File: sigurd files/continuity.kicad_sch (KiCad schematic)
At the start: 26 parts, among them U3 VN7050ASTR, U4 VN7050ASTR, U5 VN7050ASTR

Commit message: funny fortnite
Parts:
- added R33: 47k, Resistor_SMD:R_0603_1608Metric_Pad0.98x0.95mm_HandSolder, symbol Device:R_Small
- R27, R28, R32: footprint Resistor_SMD:R_0603_1608Metric -> Resistor_SMD:R_0603_1608Metric_Pad0.98x0.95mm_HandSolder
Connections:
- net JMPR: now also R33.1; no longer D3.2 (A)
- new net: D3.2 (A), R33.2
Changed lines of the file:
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@@
-	(wire
-		(pts
-			(xy 106.68 128.27) (xy 106.68 133.35)
-		)
-		(stroke
-			(width 0)
-			(type default)
-		)
-	)
 	(wire
 		(pts
@@
 	)
 	(symbol
-		(lib_id "Device:R_Small")
-		(at 102.87 95.25 270)
-		(unit 1)
-		(exclude_from_sim no)
-		(in_bom yes)
-		(on_board yes)
-		(dnp no)
-		(fields_autoplaced yes)
-		(property "Reference" "R28"
-			(at 102.87 90.17 90)
-			(effects
-				(font
-					(size 1.27 1.27)
-				)
-			)
-		)
-		(property "Value" "47k"
-			(at 102.87 92.71 90)
-			(effects
-				(font
-					(size 1.27 1.27)
-				)
-			)
-		)
-		(property "Footprint" "Resistor_SMD:R_0603_1608Metric"
-			(at 102.87 95.25 0)
-			(effects
-				(font
-					(size 1.27 1.27)
-				)
-				(hide yes)
-			)
-		)
-		(property "Datasheet" "~"
-			(at 102.87 95.25 0)
-			(effects
-				(font
-					(size 1.27 1.27)
-				)
-				(hide yes)
-			)
-		)
-		(property "Description" ""
-			(at 102.87 95.25 0)
-			(effects
-				(font
-					(size 1.27 1.27)
-				)
-				(hide yes)
-			)
-		)
-		(pin "1"
-		)
-		(pin "2"
-		)
-		(instances
-			(project "SIGURD"
-				(path "/a4a592a3-08d1-41ec-9dda-18a75407e2f6/8efa7d73-8cac-417d-b1a4-5e5d923803a7"
-					(reference "R28")
-					(unit 1)
-				)
-			)
-		)
-	)
-	(symbol
 		(lib_name "Earth_12")
 		(lib_id "power:Earth")
@@
 	)
 	(symbol
+		(lib_id "Device:R_Small")
+		(at 102.87 142.24 270)
+		(unit 1)
+		(exclude_from_sim no)
+		(in_bom yes)
+		(on_board yes)
+		(dnp no)
+		(fields_autoplaced yes)
+		(property "Reference" "R32"
+			(at 102.87 137.16 90)
+			(effects
+				(font
+					(size 1.27 1.27)
+				)
+			)
+		)
+		(property "Value" "47k"
+			(at 102.87 139.7 90)
+			(effects
+				(font
+					(size 1.27 1.27)
+				)
+			)
+		)
+		(property "Footprint" "Resistor_SMD:R_0603_1608Metric_Pad0.98x0.95mm_HandSolder"
+			(at 102.87 142.24 0)
+			(effects
+				(font
+					(size 1.27 1.27)
+				)
+				(hide yes)
+			)
+		)
+		(property "Datasheet" "~"
+			(at 102.87 142.24 0)
+			(effects
+				(font
+					(size 1.27 1.27)
+				)
+				(hide yes)
+			)
+		)
+		(property "Description" ""
+			(at 102.87 142.24 0)
+			(effects
+				(font
+					(size 1.27 1.27)
+				)
+				(hide yes)
+			)
+		)
+		(pin "1"
+		)
+		(pin "2"
+		)
+		(instances
+			(project "SIGURD"
+				(path "/a4a592a3-08d1-41ec-9dda-18a75407e2f6/8efa7d73-8cac-417d-b1a4-5e5d923803a7"
+					(reference "R32")
+					(unit 1)
+				)
+			)
+		)
+	)
+	(symbol
 		(lib_id "Device:LED")
 		(at 107.95 44.45 90)
@@
 			)
 		)
-		(property "Footprint" "Resistor_SMD:R_0603_1608Metric"
+		(property "Footprint" "Resistor_SMD:R_0603_1608Metric_Pad0.98x0.95mm_HandSolder"
 			(at 102.87 49.53 0)
 			(effects
@@
 				(path "/a4a592a3-08d1-41ec-9dda-18a75407e2f6/8efa7d73-8cac-417d-b1a4-5e5d923803a7"
 					(reference "R27")
+					(unit 1)
+				)
+			)
+		)
+	)
+	(symbol
+		(lib_id "Device:R_Small")
+		(at 102.87 95.25 270)
+		(unit 1)
+		(exclude_from_sim no)
+		(in_bom yes)
+		(on_board yes)
+		(dnp no)
+		(fields_autoplaced yes)
+		(property "Reference" "R28"
+			(at 102.87 90.17 90)
+			(effects
+				(font
+					(size 1.27 1.27)
+				)
+			)
+		)
+		(property "Value" "47k"
+			(at 102.87 92.71 90)
+			(effects
+				(font
+					(size 1.27 1.27)
+				)
+			)
+		)
+		(property "Footprint" "Resistor_SMD:R_0603_1608Metric_Pad0.98x0.95mm_HandSolder"
+			(at 102.87 95.25 0)
+			(effects
+				(font
+					(size 1.27 1.27)
+				)
+				(hide yes)
+			)
+		)
+		(property "Datasheet" "~"
+			(at 102.87 95.25 0)
+			(effects
+				(font
+					(size 1.27 1.27)
+				)
+				(hide yes)
+			)
+		)
+		(property "Description" ""
+			(at 102.87 95.25 0)
+			(effects
+				(font
+					(size 1.27 1.27)
+				)
+				(hide yes)
+			)
+		)
+		(pin "1"
+		)
+		(pin "2"
+		)
+		(instances
+			(project "SIGURD"
+				(path "/a4a592a3-08d1-41ec-9dda-18a75407e2f6/8efa7d73-8cac-417d-b1a4-5e5d923803a7"
+					(reference "R28")
 					(unit 1)
 				)
@@
 	)
 	(symbol
-		(lib_id "Device:R_Small")
-		(at 102.87 142.24 270)
-		(unit 1)
-		(exclude_from_sim no)
-		(in_bom yes)
-		(on_board yes)
-		(dnp no)
-		(fields_autoplaced yes)
-		(property "Reference" "R32"
-			(at 102.87 137.16 90)
-			(effects
-				(font
-					(size 1.27 1.27)
-				)
-			)
-		)
-		(property "Value" "47k"
-			(at 102.87 139.7 90)
-			(effects
-				(font
-					(size 1.27 1.27)
-				)
-			)
-		)
-		(property "Footprint" "Resistor_SMD:R_0603_1608Metric"
-			(at 102.87 142.24 0)
-			(effects
-				(font
-					(size 1.27 1.27)
-				)
-				(hide yes)
-			)
-		)
-		(property "Datasheet" "~"
-			(at 102.87 142.24 0)
-			(effects
-				(font
-					(size 1.27 1.27)
-				)
-				(hide yes)
-			)
-		)
-		(property "Description" ""
-			(at 102.87 142.24 0)
-			(effects
-				(font
-					(size 1.27 1.27)
-				)
-				(hide yes)
-			)
-		)
-		(pin "1"
-		)
-		(pin "2"
-		)
-		(instances
-			(project "SIGURD"
-				(path "/a4a592a3-08d1-41ec-9dda-18a75407e2f6/8efa7d73-8cac-417d-b1a4-5e5d923803a7"
-					(reference "R32")
-					(unit 1)
-				)
-			)
-		)
-	)
-	(symbol
 		(lib_id "VN7050AS:VN7050ASTR")
 		(at 176.53 41.91 0)
@@
 					(unit 1)
 				)
+			)
+		)
+	)
+	(symbol
+		(lib_id "Device:R_Small")
+		(at 106.68 130.81 0)
+		(unit 1)
+		(exclude_from_sim no)
+		(in_bom yes)
+		(on_board yes)
+		(dnp no)
+		(fields_autoplaced yes)
+		(property "Reference" "R33"
+			(at 109.22 130.175 0)
+			(effects
+				(font
+					(size 1.27 1.27)
+				)
+				(justify left)
+			)
+		)
+		(property "Value" "47k"
+			(at 109.22 132.715 0)
+			(effects
+				(font
+					(size 1.27 1.27)
+				)
+				(justify left)
+			)
+		)
+		(property "Footprint" "Resistor_SMD:R_0603_1608Metric_Pad0.98x0.95mm_HandSolder"
+			(at 106.68 130.81 0)
+			(effects
+				(font
+					(size 1.27 1.27)
+				)
+				(hide yes)
+			)
+		)
+		(property "Datasheet" "~"
+			(at 106.68 130.81 0)
+			(effects
+				(font
+					(size 1.27 1.27)
+				)
+				(hide yes)
+			)
+		)
+		(property "Description" ""
+			(at 106.68 130.81 0)
+			(effects
+				(font
+					(size 1.27 1.27)
+				)
+				(hide yes)
+			)
+		)
+		(pin "1"
+		)
+		(pin "2"
+		)
+		(instances
+			(project "SIGURD"
+				(path "/a4a592a3-08d1-41ec-9dda-18a75407e2f6/8efa7d73-8cac-417d-b1a4-5e5d923803a7"
+					(reference "R33")
+					(unit 1)
+				)

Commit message: Goober
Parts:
- F6, F7, F8: value Polyfuse -> 2.0 A
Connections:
- net VCC renamed +10V
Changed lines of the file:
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@@
 			)
 		)
-		(property "Value" "VCC"
-			(at 134.62 36.83 0)
-			(effects
-				(font
-					(size 1.27 1.27)
-				)
+		(property "Value" "+10V"
+			(at 137.16 39.3699 0)
+			(effects
+				(font
+					(size 1.27 1.27)
+				)
+				(justify left)
 			)
 		)
@@
 	)
 	(symbol
+		(lib_id "Device:Polyfuse")
+		(at 125.73 142.24 90)
+		(unit 1)
+		(exclude_from_sim no)
+		(in_bom yes)
+		(on_board yes)
+		(dnp no)
+		(fields_autoplaced yes)
+		(property "Reference" "F8"
+			(at 125.73 135.89 90)
+			(effects
+				(font
+					(size 1.27 1.27)
+				)
+			)
+		)
+		(property "Value" "2.0 A"
+			(at 125.73 138.43 90)
+			(effects
+				(font
+					(size 1.27 1.27)
+				)
+			)
+		)
+		(property "Footprint" "Fuse:Fuse_1812_4532Metric_Pad1.30x3.40mm_HandSolder"
+			(at 130.81 140.97 0)
+			(effects
+				(font
+					(size 1.27 1.27)
+				)
+				(justify left)
+				(hide yes)
+			)
+		)
+		(property "Datasheet" "~"
+			(at 125.73 142.24 0)
+			(effects
+				(font
+					(size 1.27 1.27)
+				)
+				(hide yes)
+			)
+		)
+		(property "Description" ""
+			(at 125.73 142.24 0)
+			(effects
+				(font
+					(size 1.27 1.27)
+				)
+				(hide yes)
+			)
+		)
+		(property "mfn" " 1210L150/16WR "
+			(at 125.73 142.24 90)
+			(effects
+				(font
+					(size 1.27 1.27)
+				)
+				(hide yes)
+			)
+		)
+		(pin "1"
+		)
+		(pin "2"
+		)
+		(instances
+			(project "SIGURD"
+				(path "/a4a592a3-08d1-41ec-9dda-18a75407e2f6/8efa7d73-8cac-417d-b1a4-5e5d923803a7"
+					(reference "F8")
+					(unit 1)
+				)
+			)
+		)
+	)
+	(symbol
 		(lib_id "power:VCC")
 		(at 107.95 34.29 0)
@@
 			)
 		)
-		(property "Value" "VCC"
-			(at 107.95 30.48 0)
-			(effects
-				(font
-					(size 1.27 1.27)
-				)
+		(property "Value" "+10V"
+			(at 110.49 33.0199 0)
+			(effects
+				(font
+					(size 1.27 1.27)
+				)
+				(justify left)
 			)
 		)
@@
 	)
 	(symbol
+		(lib_id "Device:Polyfuse")
+		(at 125.73 95.25 90)
+		(unit 1)
+		(exclude_from_sim no)
+		(in_bom yes)
+		(on_board yes)
+		(dnp no)
+		(fields_autoplaced yes)
+		(property "Reference" "F7"
+			(at 125.73 88.9 90)
+			(effects
+				(font
+					(size 1.27 1.27)
+				)
+			)
+		)
+		(property "Value" "2.0 A"
+			(at 125.73 91.44 90)
+			(effects
+				(font
+					(size 1.27 1.27)
+				)
+			)
+		)
+		(property "Footprint" "Fuse:Fuse_1812_4532Metric_Pad1.30x3.40mm_HandSolder"
+			(at 130.81 93.98 0)
+			(effects
+				(font
+					(size 1.27 1.27)
+				)
+				(justify left)
+				(hide yes)
+			)
+		)
+		(property "Datasheet" "~"
+			(at 125.73 95.25 0)
+			(effects
+				(font
+					(size 1.27 1.27)
+				)
+				(hide yes)
+			)
+		)
+		(property "Description" ""
+			(at 125.73 95.25 0)
+			(effects
+				(font
+					(size 1.27 1.27)
+				)
+				(hide yes)
+			)
+		)
+		(property "mfn" " 1210L150/16WR "
+			(at 125.73 95.25 90)
+			(effects
+				(font
+					(size 1.27 1.27)
+				)
+				(hide yes)
+			)
+		)
+		(pin "1"
+		)
+		(pin "2"
+		)
+		(instances
+			(project "SIGURD"
+				(path "/a4a592a3-08d1-41ec-9dda-18a75407e2f6/8efa7d73-8cac-417d-b1a4-5e5d923803a7"
+					(reference "F7")
+					(unit 1)
+				)
+			)
+		)
+	)
+	(symbol
 		(lib_id "Device:R_Small")
 		(at 187.96 91.44 0)
@@
 		(fields_autoplaced yes)
 		(property "Reference" "F6"
-			(at 125.73 44.45 90)
-			(effects
-				(font
-					(size 1.27 1.27)
-				)
-			)
-		)
-		(property "Value" "Polyfuse"
-			(at 125.73 46.99 90)
+			(at 125.73 43.18 90)
+			(effects
+				(font
+					(size 1.27 1.27)
+				)
+			)
+		)
+		(property "Value" "2.0 A"
+			(at 125.73 45.72 90)
 			(effects
 				(font
@@
 	)
 	(symbol
-		(lib_id "Device:Polyfuse")
-		(at 125.73 142.24 90)
-		(unit 1)
-		(exclude_from_sim no)
-		(in_bom yes)
-		(on_board yes)
-		(dnp no)
-		(fields_autoplaced yes)
-		(property "Reference" "F8"
-			(at 125.73 137.16 90)
-			(effects
-				(font
-					(size 1.27 1.27)
-				)
-			)
-		)
-		(property "Value" "Polyfuse"
-			(at 125.73 139.7 90)
-			(effects
-				(font
-					(size 1.27 1.27)
-				)
-			)
-		)
-		(property "Footprint" "Fuse:Fuse_1812_4532Metric_Pad1.30x3.40mm_HandSolder"
-			(at 130.81 140.97 0)
-			(effects
-				(font
-					(size 1.27 1.27)
-				)
-				(justify left)
-				(hide yes)
-			)
-		)
-		(property "Datasheet" "~"
-			(at 125.73 142.24 0)
-			(effects
-				(font
-					(size 1.27 1.27)
-				)
-				(hide yes)
-			)
-		)
-		(property "Description" ""
-			(at 125.73 142.24 0)
-			(effects
-				(font
-					(size 1.27 1.27)
-				)
-				(hide yes)
-			)
-		)
-		(property "Field4" ""
-			(at 125.73 142.24 90)
-			(effects
-				(font
-					(size 1.27 1.27)
-				)
-				(hide yes)
-			)
-		)
-		(property "mfn" " 1210L150/16WR "
-			(at 125.73 142.24 0)
-			(effects
-				(font
-					(size 1.27 1.27)
-				)
-				(hide yes)
-			)
-		)
-		(pin "1"
-		)
-		(pin "2"
-		)
-		(instances
-			(project "SIGURD"
-				(path "/a4a592a3-08d1-41ec-9dda-18a75407e2f6/8efa7d73-8cac-417d-b1a4-5e5d923803a7"
-					(reference "F8")
-					(unit 1)
-				)
-			)
-		)
-	)
-	(symbol
 		(lib_id "Device:R_Small")
 		(at 179.07 142.24 90)
@@
 					(unit 1)
 				)
-			)
-		)
-	)
-	(symbol
-		(lib_id "Device:Polyfuse")
-		(at 125.73 95.25 90)
-		(unit 1)
-		(exclude_from_sim no)
-		(in_bom yes)
-		(on_board yes)
-		(dnp no)
-		(fields_autoplaced yes)
-		(property "Reference" "F7"
-			(at 125.73 90.17 90)
-			(effects
-				(font
-					(size 1.27 1.27)
-				)
-			)
-		)
-		(property "Value" "Polyfuse"
-			(at 125.73 92.71 90)
-			(effects
-				(font
-					(size 1.27 1.27)
-				)
-			)
-		)
-		(property "Footprint" "Fuse:Fuse_1812_4532Metric_Pad1.30x3.40mm_HandSolder"
-			(at 130.81 93.98 0)
-			(effects
-				(font
-					(size 1.27 1.27)
-				)
-				(justify left)
-				(hide yes)
-			)
-		)
-		(property "Datasheet" "~"
-			(at 125.73 95.25 0)
-			(effects
-				(font
-					(size 1.27 1.27)
-				)
-				(hide yes)
-			)
-		)
-		(property "Description" ""
-			(at 125.73 95.25 0)
-			(effects
-				(font
-					(size 1.27 1.27)
-				)
-				(hide yes)
-			)
-		)
-		(property "Field4" ""
-			(at 125.73 95.25 90)
-			(effects
-				(font
-					(size 1.27 1.27)
-				)
-				(hide yes)
-			)
-		)
-		(property "mfn" " 1210L150/16WR "
-			(at 125.73 95.25 0)
-			(effects
-				(font
-					(size 1.27 1.27)
-				)
-				(hide yes)
-			)
-		)
-		(pin "1"
-		)
-		(pin "2"
-		)
-		(instances
-			(project "SIGURD"
-				(path "/a4a592a3-08d1-41ec-9dda-18a75407e2f6/8efa7d73-8cac-417d-b1a4-5e5d923803a7"
-					(reference "F7")
-					(unit 1)
-				)

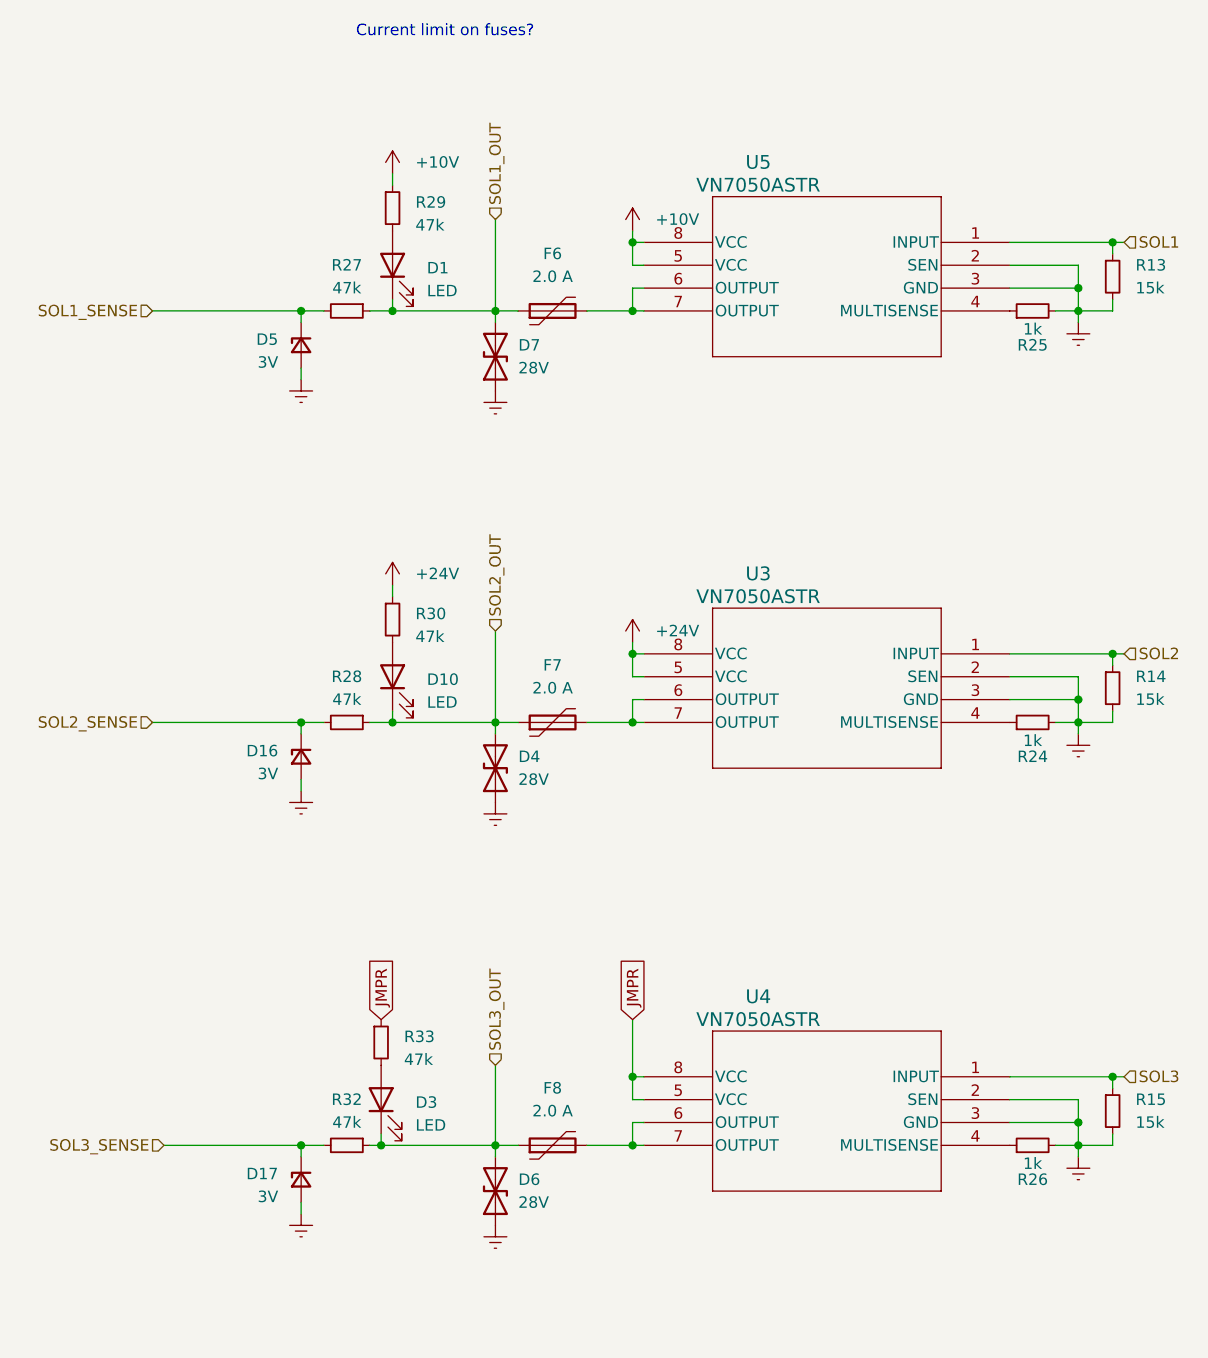
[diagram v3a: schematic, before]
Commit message: Everything but power traces routed
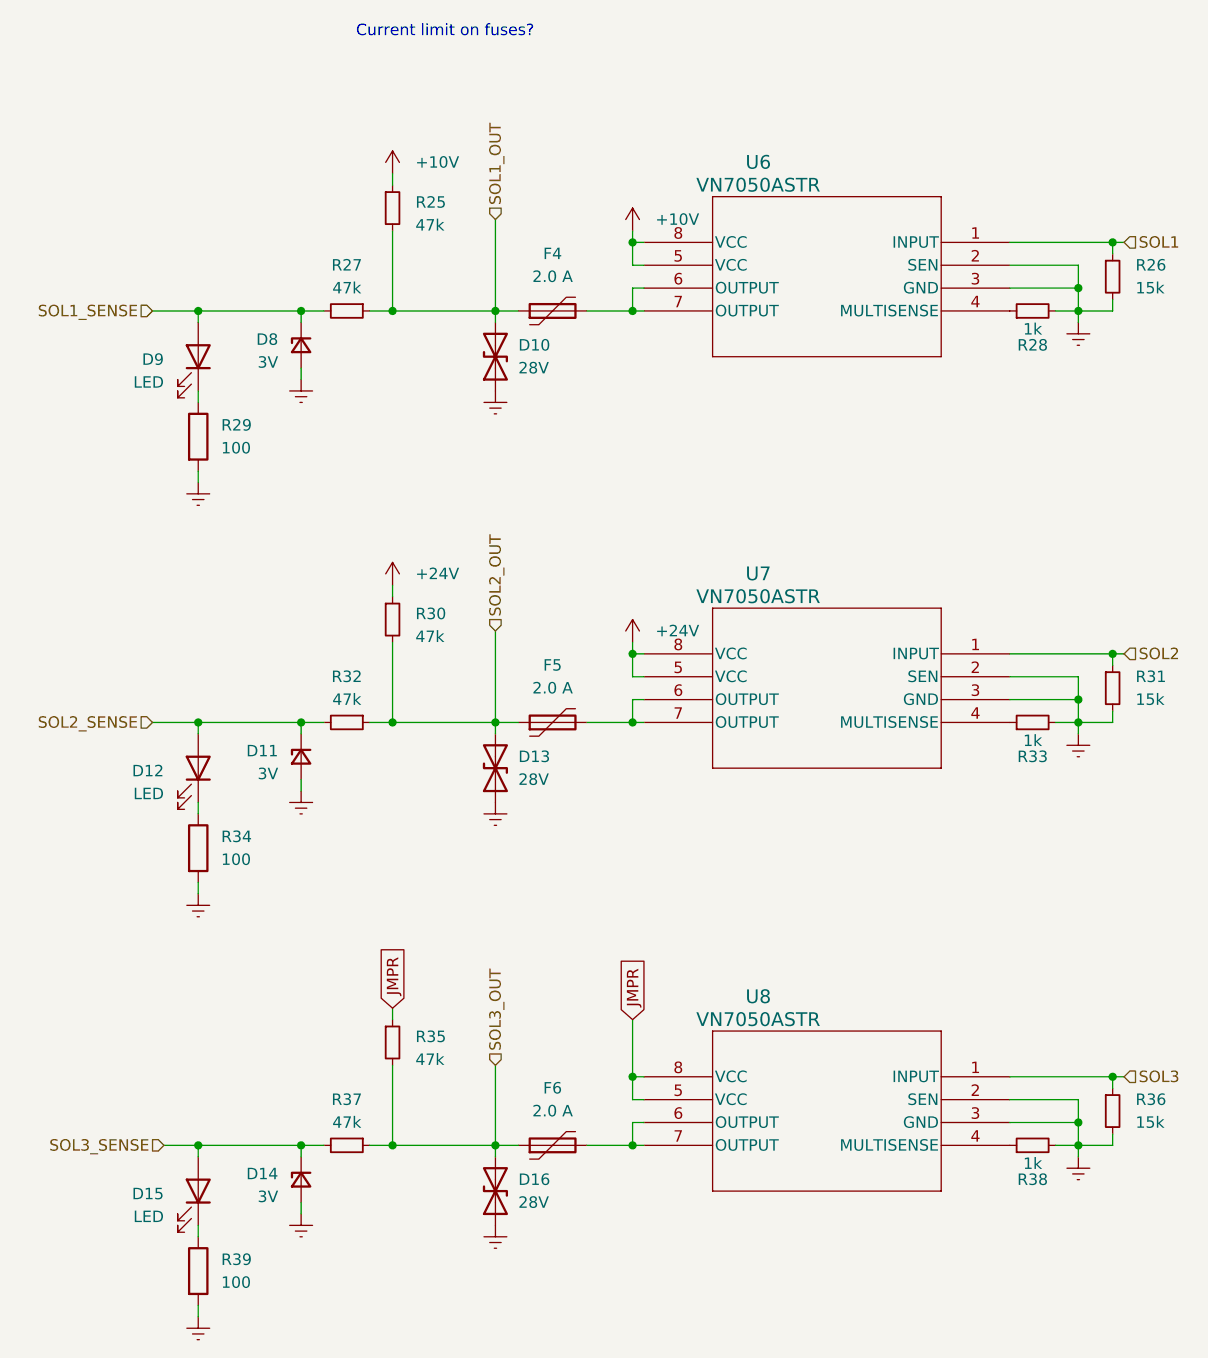
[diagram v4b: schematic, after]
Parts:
- removed D10, D3: LED, LED_SMD:LED_0603_1608Metric_Pad1.05x0.95mm_HandSolder, symbol Device:LED
- removed F7, F8: 2.0 A, Fuse:Fuse_1812_4532Metric_Pad1.30x3.40mm_HandSolder, symbol Device:Polyfuse
- added D12, D15: LED, LED_SMD:LED_0603_1608Metric_Pad1.05x0.95mm_HandSolder, symbol Device:LED
- added F5, F6: 2.0 A, Fuse:Fuse_1812_4532Metric, symbol Device:Polyfuse
- added R29, R34, R39: 100, Resistor_SMD:R_0603_1608Metric, symbol Device:R
- F4: renamed from F6; footprint Fuse:Fuse_1812_4532Metric_Pad1.30x3.40mm_HandSolder -> Fuse:Fuse_1812_4532Metric
- renumbered D7 to D10, D16 to D11, D4 to D13, D17 to D14, D6 to D16, D5 to D8, D1 to D9, R29 to R25, R13 to R26, R25 to R28, R14 to R31, R28 to R32, R24 to R33, R33 to R35, R15 to R36, R32 to R37, R26 to R38, U5 to U6, U3 to U7, U4 to U8
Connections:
- net Earth: now also R29.2, R34.2, R39.2
- net SOL1_OUT: now also R25.2; no longer D9.1 (K)
- net SOL1_SENSE: now also D9.2 (A)
- net SOL2_OUT: now also R30.2, F5.1
- net SOL2_SENSE: now also D12.2 (A)
- net SOL3_OUT: now also R35.2, F6.1
- net SOL3_SENSE: now also D15.2 (A)
- net at U8.6 (OUTPUT), U8.7 (OUTPUT): now also F6.2
- net at U7.6 (OUTPUT), U7.7 (OUTPUT): now also F5.2
- new net: D15.1 (K), R39.1
- new net: D12.1 (K), R34.1
- new net: D9.1 (K), R29.1
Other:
- moved on the sheet: D9, R35
